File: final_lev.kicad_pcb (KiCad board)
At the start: 2 copper layers, 60 parts, among them Q1 IRF100B201, Q2 IRF100B201, Q3 IRF100B201, Q4 IRF100B201, U1 IR2184, U2 IR2184, U3 INA240A1D, U4 LM393, U5 74HC74

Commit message: clean rollback
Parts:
- added C101: 470uF, Capacitor_THT:CP_Radial_D18.0mm_P7.50mm, F.Cu at (30.1, 42.8)
- added C102: 470uF, Capacitor_THT:CP_Radial_D18.0mm_P7.50mm, F.Cu at (30.1, 62.3)
- added C103: 470uF, Capacitor_THT:CP_Radial_D18.0mm_P7.50mm, F.Cu at (30.1, 81.9)
- added C104: 470uF, Capacitor_THT:CP_Radial_D18.0mm_P7.50mm, F.Cu at (30.1, 101.4)
- added C105: 470uF, Capacitor_THT:CP_Radial_D18.0mm_P7.50mm, F.Cu at (30.1, 121.0)
- added C106: 470uF, Capacitor_THT:CP_Radial_D18.0mm_P7.50mm, F.Cu at (30.1, 140.5)
- added C201: 220uF, Capacitor_THT:CP_Radial_D8.0mm_P3.50mm, F.Cu at (120.4, 49.7)
- added C202: 220uF, Capacitor_THT:CP_Radial_D8.0mm_P3.50mm, F.Cu at (120.4, 59.3)
- added C203: 10uF, Capacitor_SMD:C_1206_3216Metric_Pad1.33x1.80mm_HandSolder, F.Cu at (120.2, 84.1)
- added C204: 100nF, Capacitor_SMD:C_0805_2012Metric_Pad1.18x1.45mm_HandSolder, F.Cu at (114.7, 46.5)
- added C205: 100nF, Capacitor_SMD:C_0805_2012Metric_Pad1.18x1.45mm_HandSolder, F.Cu at (114.7, 49.5)
- added C206: 100nF, Capacitor_SMD:C_0805_2012Metric_Pad1.18x1.45mm_HandSolder, F.Cu at (114.7, 52.5)
- added C207: 100nF, Capacitor_SMD:C_0805_2012Metric_Pad1.18x1.45mm_HandSolder, F.Cu at (114.7, 55.5)
- added C208: 100nF, Capacitor_SMD:C_0805_2012Metric_Pad1.18x1.45mm_HandSolder, F.Cu at (114.7, 58.5)
- added C209: 100nF, Capacitor_SMD:C_0805_2012Metric_Pad1.18x1.45mm_HandSolder, F.Cu at (114.7, 61.5)
- added C210: 100nF, Capacitor_SMD:C_0805_2012Metric_Pad1.18x1.45mm_HandSolder, F.Cu at (114.7, 64.5)
- added C211: 1nF, Capacitor_SMD:C_0805_2012Metric_Pad1.18x1.45mm_HandSolder, F.Cu at (105.0, 112.7)
- added C212: 1uF, Capacitor_SMD:C_1210_3225Metric_Pad1.33x2.70mm_HandSolder, F.Cu at (79.6, 92.6)
- added C213: 100nF, Capacitor_SMD:C_0805_2012Metric_Pad1.18x1.45mm_HandSolder, F.Cu at (105.0, 115.7)
- added C214: 1uF, Capacitor_SMD:C_1210_3225Metric_Pad1.33x2.70mm_HandSolder, F.Cu at (79.6, 96.9)
- added C215: 1uF, Capacitor_SMD:C_1210_3225Metric_Pad1.33x2.70mm_HandSolder, F.Cu at (79.6, 101.1)
- added C216: 1uF, Capacitor_SMD:C_1210_3225Metric_Pad1.33x2.70mm_HandSolder, F.Cu at (79.6, 105.4)
- added C217: 100nF, Capacitor_SMD:C_0805_2012Metric_Pad1.18x1.45mm_HandSolder, F.Cu at (105.0, 118.7)
- added C218: 100nF, Capacitor_SMD:C_0805_2012Metric_Pad1.18x1.45mm_HandSolder, F.Cu at (105.0, 121.7)
- added C219: 1uF, Capacitor_SMD:C_1210_3225Metric_Pad1.33x2.70mm_HandSolder, F.Cu at (79.6, 109.6)
- added C220: 1uF, Capacitor_SMD:C_1210_3225Metric_Pad1.33x2.70mm_HandSolder, F.Cu at (79.6, 113.9)
- added C221: 1uF, Capacitor_SMD:C_1210_3225Metric_Pad1.33x2.70mm_HandSolder, F.Cu at (79.6, 118.1)
- added C222: 1uF, Capacitor_SMD:C_1210_3225Metric_Pad1.33x2.70mm_HandSolder, F.Cu at (79.6, 122.4)
- added C223: 100nF, Capacitor_SMD:C_0805_2012Metric_Pad1.18x1.45mm_HandSolder, F.Cu at (105.0, 124.7)
- added C224: 100nF, Capacitor_SMD:C_0805_2012Metric_Pad1.18x1.45mm_HandSolder, F.Cu at (109.8, 112.7)
- added C225: 100nF, Capacitor_SMD:C_0805_2012Metric_Pad1.18x1.45mm_HandSolder, F.Cu at (109.8, 115.7)
- added C226: 1uF, Capacitor_SMD:C_0805_2012Metric_Pad1.18x1.45mm_HandSolder, F.Cu at (109.8, 118.7)
- added C227: 1uF, Capacitor_SMD:C_0805_2012Metric_Pad1.18x1.45mm_HandSolder, F.Cu at (109.8, 121.7)
- added C228: 100nF, Capacitor_SMD:C_0805_2012Metric_Pad1.18x1.45mm_HandSolder, F.Cu at (109.8, 124.7)
- added C229: 100nF, Capacitor_SMD:C_0805_2012Metric_Pad1.18x1.45mm_HandSolder, F.Cu at (114.6, 112.7)
- added C230: 1uF, Capacitor_SMD:C_0805_2012Metric_Pad1.18x1.45mm_HandSolder, F.Cu at (114.6, 115.7)
- added C231: 1uF, Capacitor_SMD:C_0805_2012Metric_Pad1.18x1.45mm_HandSolder, F.Cu at (114.6, 118.7)
- added D201: SS34, Diode_SMD:D_SMA_Handsoldering, F.Cu at (122.2, 66.3)
- added D202: SS34, Diode_SMD:D_SMA_Handsoldering, F.Cu at (122.2, 70.9)
- added D203: 1N4148W, Diode_SMD:D_SOD-123, F.Cu at (111.3, 92.2)
- added D204: 1N4148W, Diode_SMD:D_SOD-123, F.Cu at (111.3, 95.5)
- added D205: 5.0SMDJ70A, Diode_SMD:D_SMC_Handsoldering, F.Cu at (110.1, 130.1)
- added D206: 1N4148W, Diode_SMD:D_SOD-123, F.Cu at (111.3, 98.9)
- added D207: 1N4148W, Diode_SMD:D_SOD-123, F.Cu at (111.3, 102.2)
- added D208: ES1D, Diode_SMD:D_SMA_Handsoldering, F.Cu at (87.7, 116.6)
- added D209: ES1D, Diode_SMD:D_SMA_Handsoldering, F.Cu at (87.7, 121.1)
- added J101: +60V IN, lev_lib:389690002, F.Cu at (52.7, 40.6)
- added J201: RAILS IN, Connector_Molex:Molex_Micro-Fit_3.0_43650-0400_1x04_P3.00mm_Horizontal, F.Cu at (131.2, 54.9)
- added J202: CONTROL, Connector_Molex:Molex_Micro-Fit_3.0_43650-1200_1x12_P3.00mm_Horizontal, F.Cu at (111.9, 42.9)
- added J203: YOKE 1, lev_lib:389690002, F.Cu at (85.7, 40.6)
- added J204: YOKE 2, lev_lib:389690002, F.Cu at (85.7, 68.3)
- added Q201: IRF100B201, Package_TO_SOT_THT:TO-220-3_Vertical, F.Cu at (85.8, 94.4)
- added Q202: IRF100B201, Package_TO_SOT_THT:TO-220-3_Vertical, F.Cu at (85.8, 100.4)
- added Q203: IRF100B201, Package_TO_SOT_THT:TO-220-3_Vertical, F.Cu at (85.8, 106.3)
- added Q204: IRF100B201, Package_TO_SOT_THT:TO-220-3_Vertical, F.Cu at (85.8, 112.3)
- added R101: 22k, Resistor_SMD:R_1206_3216Metric_Pad1.30x1.75mm_HandSolder, F.Cu at (46.6, 62.4)
- added R201: 10k, Resistor_SMD:R_0805_2012Metric_Pad1.20x1.40mm_HandSolder, F.Cu at (110.0, 46.4)
- added R202: 10k, Resistor_SMD:R_0805_2012Metric_Pad1.20x1.40mm_HandSolder, F.Cu at (110.0, 49.4)
- added R203: 10k, Resistor_SMD:R_0805_2012Metric_Pad1.20x1.40mm_HandSolder, F.Cu at (110.0, 52.3)
- added R204: 10k, Resistor_SMD:R_0805_2012Metric_Pad1.20x1.40mm_HandSolder, F.Cu at (110.0, 55.3)
- added R205: 100R, Resistor_SMD:R_0805_2012Metric_Pad1.20x1.40mm_HandSolder, F.Cu at (110.0, 58.2)
- added R206: 100R, Resistor_SMD:R_0805_2012Metric_Pad1.20x1.40mm_HandSolder, F.Cu at (110.0, 61.2)
- added R207: 100R, Resistor_SMD:R_0805_2012Metric_Pad1.20x1.40mm_HandSolder, F.Cu at (110.0, 64.1)
- added R208: 100R, Resistor_SMD:R_0805_2012Metric_Pad1.20x1.40mm_HandSolder, F.Cu at (110.0, 67.1)
- added R209: 100R, Resistor_SMD:R_0805_2012Metric_Pad1.20x1.40mm_HandSolder, F.Cu at (110.0, 70.0)
- added R210: 10R, Resistor_SMD:R_0805_2012Metric_Pad1.20x1.40mm_HandSolder, F.Cu at (96.5, 92.0)
- added R211: 10R, Resistor_SMD:R_0805_2012Metric_Pad1.20x1.40mm_HandSolder, F.Cu at (96.5, 94.9)
- added R212: 4.7R, Resistor_SMD:R_0805_2012Metric_Pad1.20x1.40mm_HandSolder, F.Cu at (96.5, 97.9)
- added R213: 4.7R, Resistor_SMD:R_0805_2012Metric_Pad1.20x1.40mm_HandSolder, F.Cu at (96.5, 100.8)
- added R214: 10R, Resistor_SMD:R_1206_3216Metric_Pad1.30x1.75mm_HandSolder, F.Cu at (117.2, 92.2)
- added R215: 10R, Resistor_SMD:R_1206_3216Metric_Pad1.30x1.75mm_HandSolder, F.Cu at (117.2, 95.5)
- added R216: 10k, Resistor_SMD:R_0805_2012Metric_Pad1.20x1.40mm_HandSolder, F.Cu at (96.5, 103.8)
- added R217: 10k, Resistor_SMD:R_0805_2012Metric_Pad1.20x1.40mm_HandSolder, F.Cu at (96.5, 106.7)
- added R218: 10k, Resistor_SMD:R_0805_2012Metric_Pad1.20x1.40mm_HandSolder, F.Cu at (96.5, 109.7)
- added R219: 1m, Resistor_SMD:R_Shunt_Vishay_WSK2512_6332Metric_T2.66mm, F.Cu at (113.3, 106.3)
- added R220: 24k, Resistor_SMD:R_0805_2012Metric_Pad1.20x1.40mm_HandSolder, F.Cu at (101.3, 92.0)
- added R221: 10k, Resistor_SMD:R_0805_2012Metric_Pad1.20x1.40mm_HandSolder, F.Cu at (101.3, 94.9)
- added R222: 10k, Resistor_SMD:R_0805_2012Metric_Pad1.20x1.40mm_HandSolder, F.Cu at (101.3, 97.9)
- added R223: 10k, Resistor_SMD:R_0805_2012Metric_Pad1.20x1.40mm_HandSolder, F.Cu at (101.3, 100.8)
- added R224: 10k, Resistor_SMD:R_0805_2012Metric_Pad1.20x1.40mm_HandSolder, F.Cu at (101.3, 103.8)
- added R225: 10k, Resistor_SMD:R_0805_2012Metric_Pad1.20x1.40mm_HandSolder, F.Cu at (101.3, 106.7)
- added R226: 10R, Resistor_SMD:R_1206_3216Metric_Pad1.30x1.75mm_HandSolder, F.Cu at (117.2, 98.8)
- added R227: 10R, Resistor_SMD:R_1206_3216Metric_Pad1.30x1.75mm_HandSolder, F.Cu at (117.2, 102.1)
- added R228: 4.7R, Resistor_SMD:R_0805_2012Metric_Pad1.20x1.40mm_HandSolder, F.Cu at (101.3, 109.7)
- added R229: 4.7R, Resistor_SMD:R_0805_2012Metric_Pad1.20x1.40mm_HandSolder, F.Cu at (106.0, 92.0)
- added R230: 10k, Resistor_SMD:R_0805_2012Metric_Pad1.20x1.40mm_HandSolder, F.Cu at (106.0, 94.9)
- added R231: 1R, Resistor_SMD:R_0805_2012Metric_Pad1.20x1.40mm_HandSolder, F.Cu at (106.0, 97.9)
- added R232: 1R, Resistor_SMD:R_0805_2012Metric_Pad1.20x1.40mm_HandSolder, F.Cu at (106.0, 100.8)
- added U201: 74LVC2G17, Package_TO_SOT_SMD:SOT-23-6, F.Cu at (119.7, 75.6)
- added U202: 74LVC2G17, Package_TO_SOT_SMD:SOT-23-6, F.Cu at (119.7, 80.2)
- added U203: INA240A1D, Package_SO:SOIC-8_3.9x4.9mm_P1.27mm, F.Cu at (98.4, 114.5)
- added U204: LM393, Package_SO:SOIC-8_3.9x4.9mm_P1.27mm, F.Cu at (98.4, 121.1)
- added U205: 74HC74, Package_SO:SOIC-14_3.9x8.7mm_P1.27mm, F.Cu at (86.8, 128.7)
- added U206: IR2184, Package_SO:SOIC-8_3.9x4.9mm_P1.27mm, F.Cu at (98.4, 127.7)
- added U207: IR2184, Package_SO:SOIC-8_3.9x4.9mm_P1.27mm, F.Cu at (98.4, 134.3)
- moved C16 89.6 mm to (155.4, 112.7)
- moved C17 89.6 mm to (155.4, 115.7)
- moved C18 89.6 mm to (155.4, 118.7)
- moved C19 89.6 mm to (155.4, 121.7)
- moved C20 89.6 mm to (155.4, 124.7)
- moved C21 89.6 mm to (160.2, 112.7)
- moved C22 89.6 mm to (160.2, 115.7)
- moved C23 89.6 mm to (160.2, 118.7)
- moved D5 89.6 mm to (156.9, 95.5)
- moved R9 89.6 mm to (162.7, 98.8)
- moved U1 89.6 mm to (143.9, 114.5)
- moved U2 89.6 mm to (143.9, 121.1)
- moved U3 89.6 mm to (143.9, 127.7)
- moved U4 89.6 mm to (143.9, 134.3)
- moved C1 89.6 mm to (150.6, 112.7)
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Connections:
- net /power_channel/FAULT_N renamed /CH1/FAULT_N
- net /power_channel/G_Q1 renamed /CH1/G_Q1
- net /power_channel/G_Q2 renamed /CH1/G_Q2
- net /power_channel/G_Q3 renamed /CH1/G_Q3
- net /power_channel/G_Q4 renamed /CH1/G_Q4
- net /power_channel/HO_A renamed /CH1/HO_A
- net /power_channel/HO_B renamed /CH1/HO_B
- net /power_channel/ISNS renamed /ISNS1
- net /power_channel/LO_A renamed /CH1/LO_A
- net /power_channel/LO_B renamed /CH1/LO_B
- net /power_channel/RESET renamed /RESET
- net /power_channel/SD renamed /CH1/SD
- net /power_channel/SNS_N renamed /CH1/SNS_N
- net /power_channel/SNS_N_F renamed /CH1/SNS_N_F
- net /power_channel/SNS_P renamed /CH1/SNS_P
- net /power_channel/SNS_P_F renamed /CH1/SNS_P_F
- net /power_channel/SW_A renamed /CH1/SW_A
- net /power_channel/SW_B renamed /COIL_B1
- net /power_channel/VB_A renamed /CH1/VB_A
- net /power_channel/VB_B renamed /CH1/VB_B
- net /power_channel/VTH_HI renamed /CH1/VTH_HI
- net /power_channel/VTH_LO renamed /CH1/VTH_LO
- R11 pad 4: /power_channel/COIL_A -> /COIL_A1
- U1 pad 1: /power_channel/PWM_A -> /PWM_A1
- U2 pad 1: /power_channel/PWM_B -> /PWM_B1
- U5 pad 5: /power_channel/FAULT -> /FAULT1

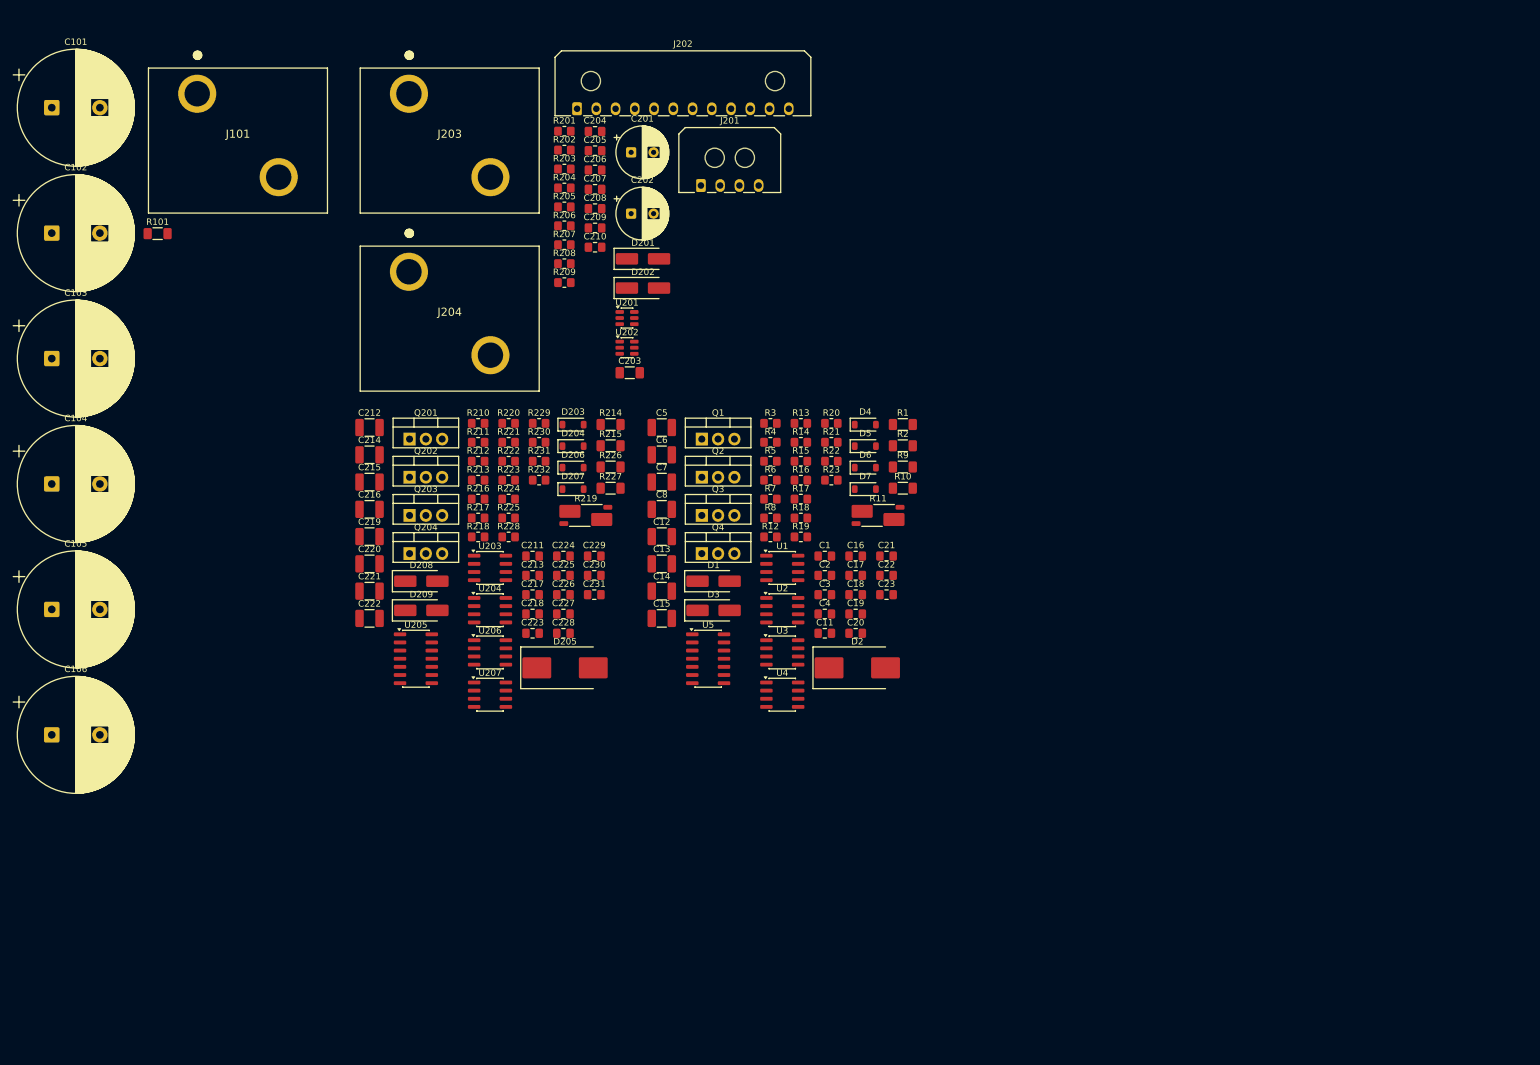
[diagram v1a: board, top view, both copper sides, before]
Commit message: Adversarial review fixes: set-dominant latch, MCU enable, 3V3 hold-up, sense chain, 16-way connector
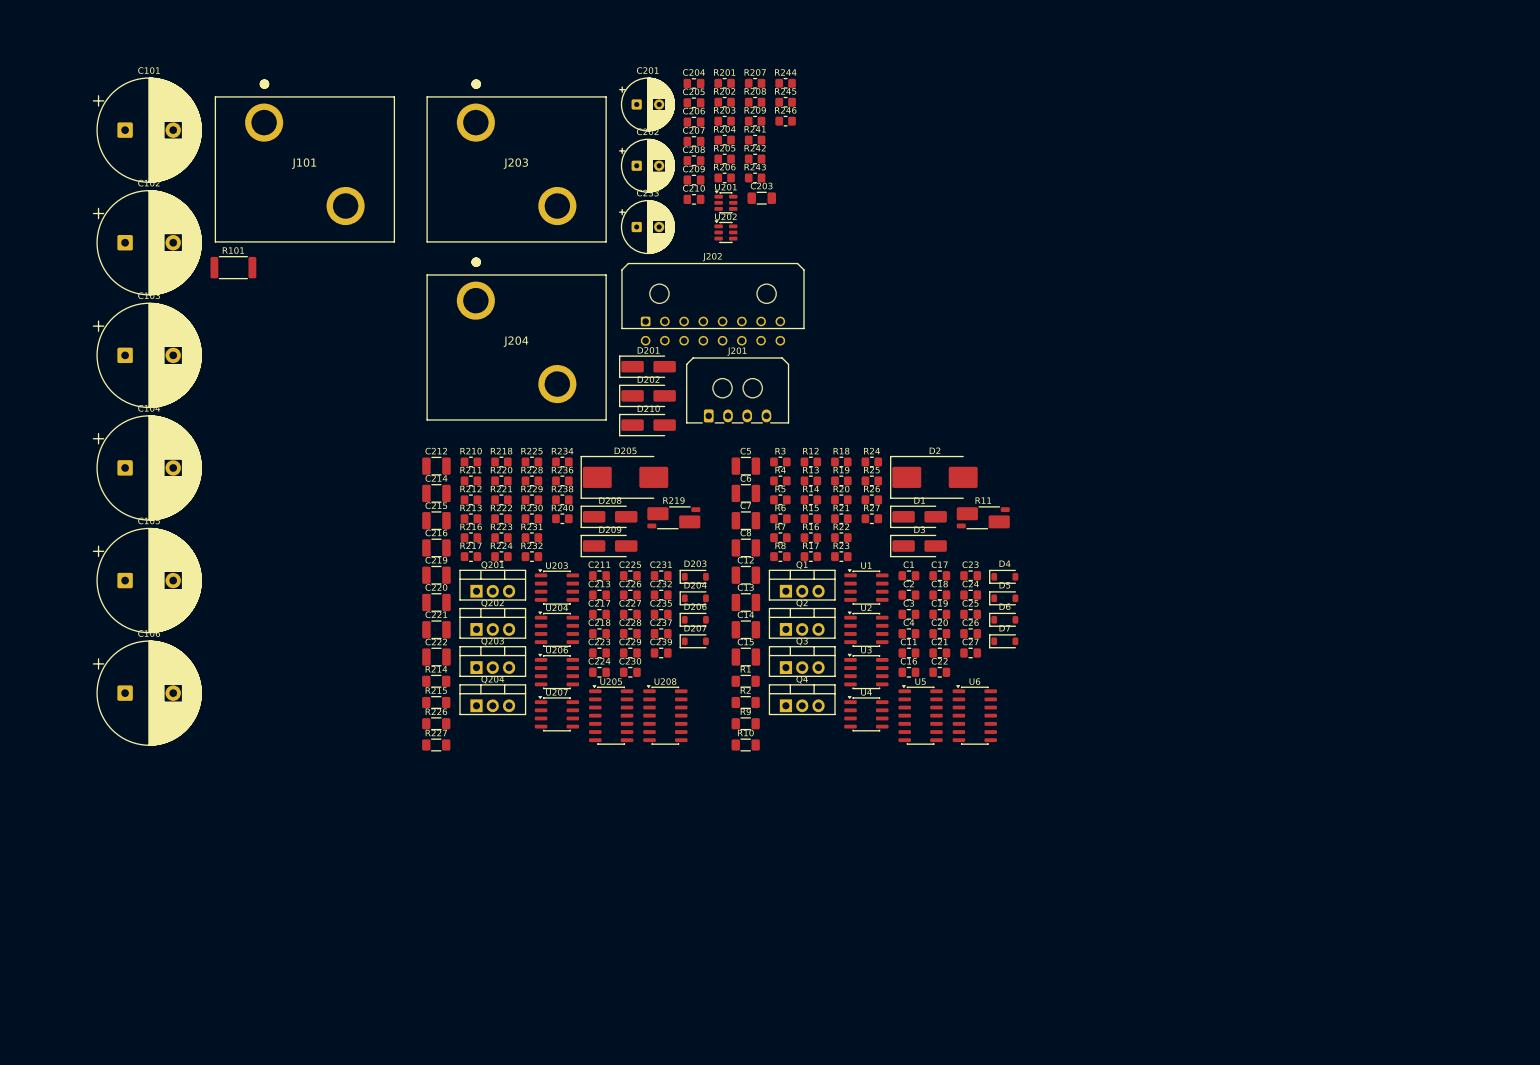
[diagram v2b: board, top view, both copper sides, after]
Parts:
- added C232: 100nF, Capacitor_SMD:C_0805_2012Metric_Pad1.18x1.45mm_HandSolder, F.Cu at (125.1, 118.7)
- added C233: 220uF, Capacitor_THT:CP_Radial_D8.0mm_P3.50mm, F.Cu at (121.2, 61.4)
- added C235: 100nF, Capacitor_SMD:C_0805_2012Metric_Pad1.18x1.45mm_HandSolder, F.Cu at (125.1, 121.7)
- added C237: 100nF, Capacitor_SMD:C_0805_2012Metric_Pad1.18x1.45mm_HandSolder, F.Cu at (125.1, 124.8)
- added C239: 4.7nF, Capacitor_SMD:C_0805_2012Metric_Pad1.18x1.45mm_HandSolder, F.Cu at (125.1, 127.8)
- added C24: 100nF, Capacitor_SMD:C_0805_2012Metric_Pad1.18x1.45mm_HandSolder, F.Cu at (173.3, 118.7)
- added C25: 100nF, Capacitor_SMD:C_0805_2012Metric_Pad1.18x1.45mm_HandSolder, F.Cu at (173.3, 121.7)
- added C26: 100nF, Capacitor_SMD:C_0805_2012Metric_Pad1.18x1.45mm_HandSolder, F.Cu at (173.3, 124.8)
- added C27: 4.7nF, Capacitor_SMD:C_0805_2012Metric_Pad1.18x1.45mm_HandSolder, F.Cu at (173.3, 127.8)
- added D210: SS34, Diode_SMD:D_SMA_Handsoldering, F.Cu at (123.1, 92.2)
- added R234: 3.3k, Resistor_SMD:R_0805_2012Metric_Pad1.20x1.40mm_HandSolder, F.Cu at (109.7, 98.0)
- added R236: 10k, Resistor_SMD:R_0805_2012Metric_Pad1.20x1.40mm_HandSolder, F.Cu at (109.7, 100.9)
- added R238: 10k, Resistor_SMD:R_0805_2012Metric_Pad1.20x1.40mm_HandSolder, F.Cu at (109.7, 103.9)
- added R24: 10k, Resistor_SMD:R_0805_2012Metric_Pad1.20x1.40mm_HandSolder, F.Cu at (157.9, 98.0)
- added R240: 1k, Resistor_SMD:R_0805_2012Metric_Pad1.20x1.40mm_HandSolder, F.Cu at (109.7, 106.8)
- added R241: 15k, Resistor_SMD:R_0805_2012Metric_Pad1.20x1.40mm_HandSolder, F.Cu at (139.7, 47.8)
- added R242: 15k, Resistor_SMD:R_0805_2012Metric_Pad1.20x1.40mm_HandSolder, F.Cu at (139.7, 50.8)
- added R243: 100R, Resistor_SMD:R_0805_2012Metric_Pad1.20x1.40mm_HandSolder, F.Cu at (139.7, 53.7)
- added R244: 10k, Resistor_SMD:R_0805_2012Metric_Pad1.20x1.40mm_HandSolder, F.Cu at (144.4, 39.0)
- added R245: 100R, Resistor_SMD:R_0805_2012Metric_Pad1.20x1.40mm_HandSolder, F.Cu at (144.4, 41.9)
- added R246: 10k, Resistor_SMD:R_0805_2012Metric_Pad1.20x1.40mm_HandSolder, F.Cu at (144.4, 44.9)
- added R25: 10k, Resistor_SMD:R_0805_2012Metric_Pad1.20x1.40mm_HandSolder, F.Cu at (157.9, 100.9)
- added R26: 3.3k, Resistor_SMD:R_0805_2012Metric_Pad1.20x1.40mm_HandSolder, F.Cu at (157.9, 103.9)
- added R27: 1k, Resistor_SMD:R_0805_2012Metric_Pad1.20x1.40mm_HandSolder, F.Cu at (157.9, 106.8)
- added U208: 74HCT00, Package_SO:SOIC-14_3.9x8.7mm_P1.27mm, F.Cu at (125.7, 137.5)
- added U6: 74HCT00, Package_SO:SOIC-14_3.9x8.7mm_P1.27mm, F.Cu at (173.9, 137.5)
- C101, C102, C103, C104, C105, C106: footprint Capacitor_THT:CP_Radial_D18.0mm_P7.50mm -> Capacitor_THT:CP_Radial_D16.0mm_P7.50mm
- J202: value CONTROL -> Conn_02x08_Odd_Even; footprint Connector_Molex:Molex_Micro-Fit_3.0_43650-1200_1x12_P3.00mm_Horizontal -> Connector_Molex:Molex_Micro-Fit_3.0_43045-1600_2x08_P3.00mm_Horizontal
- R101: footprint Resistor_SMD:R_1206_3216Metric_Pad1.30x1.75mm_HandSolder -> Resistor_SMD:R_2512_6332Metric
- R11, R219: value 1m -> 0.5m
- R15, R220: value 24k -> 43k
- R206, R207: value 100R -> 10k
- U203, U3: value INA240A1D -> INA240A2D
- U204, U4: value LM393 -> LM2903B
- U205, U5: value 74HC74 -> 74HCT74
- moved R214 48.4 mm to (90.0, 132.2)
- moved R215 48.4 mm to (90.0, 135.5)
- moved R227 48.4 mm to (90.0, 142.1)
- moved R226 48.4 mm to (90.0, 138.8)
- moved R1 46.9 mm to (138.2, 132.2)
- moved R2 46.9 mm to (138.2, 135.5)
- moved R10 46.9 mm to (138.2, 142.1)
- moved R9 46.9 mm to (138.2, 138.8)
- moved R207 38.9 mm to (139.7, 39.0)
- moved R208 38.9 mm to (139.7, 41.9)
- moved R209 38.9 mm to (139.7, 44.9)
- moved J201 35.9 mm to (132.5, 90.8)
- moved J202 34.8 mm to (122.6, 76.1)
- moved U5 34.3 mm to (165.5, 137.5)
- moved C203 34.1 mm to (140.7, 56.9)
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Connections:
- J201 pad 3: +3.3V -> /IO_PROTECT/+3V3_IN
- J202 pad 10: /IO_PROTECT/ISNS1_OUT -> /IO_PROTECT/EN2_IN
- J202 pad 11: /IO_PROTECT/ISNS2_OUT -> /IO_PROTECT/RESET_IN
- J202 pad 12: GND -> /IO_PROTECT/OK1_OUT
- J202 pad 2: /IO_PROTECT/PWM_A1_IN -> GND
- J202 pad 3: /IO_PROTECT/PWM_B1_IN -> /IO_PROTECT/PWM_A1_IN
- J202 pad 5: /IO_PROTECT/PWM_B2_IN -> /IO_PROTECT/PWM_B1_IN
- J202 pad 6: GND -> /IO_PROTECT/PWM_B2_IN
- J202 pad 7: /IO_PROTECT/RESET_IN -> GND
- J202 pad 8: /IO_PROTECT/FAULT1_OUT -> GND
- J202 pad 9: /IO_PROTECT/FAULT2_OUT -> /IO_PROTECT/EN1_IN
- R206 pad 1: /IO_PROTECT/FAULT1_OUT -> /IO_PROTECT/OK1_OUT
- R206 pad 2: /FAULT1 -> /OK1
- R207 pad 1: /IO_PROTECT/FAULT2_OUT -> /IO_PROTECT/OK2_OUT
- R207 pad 2: /FAULT2 -> /OK2
- U204 pad 2: /ISNS2 -> /CH2/ISNS_F
- U204 pad 5: /ISNS2 -> /CH2/ISNS_F
- U205 pad 1: /RESET -> /CH2/RESET_EFF
- U205 pad 5: /FAULT2 -> unconnected-(U205A-Q-Pad5)
- U205 pad 6: /CH2/SD -> /CH2/SD_Q
- U4 pad 2: /ISNS1 -> /CH1/ISNS_F
- U4 pad 5: /ISNS1 -> /CH1/ISNS_F
- U5 pad 1: /RESET -> /CH1/RESET_EFF
- U5 pad 5: /FAULT1 -> unconnected-(U5A-Q-Pad5)
- U5 pad 6: /CH1/SD -> /CH1/SD_Q

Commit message: A14 modulation commitment (unipolar 3-level, 180 deg interleave); title blocks refreshed
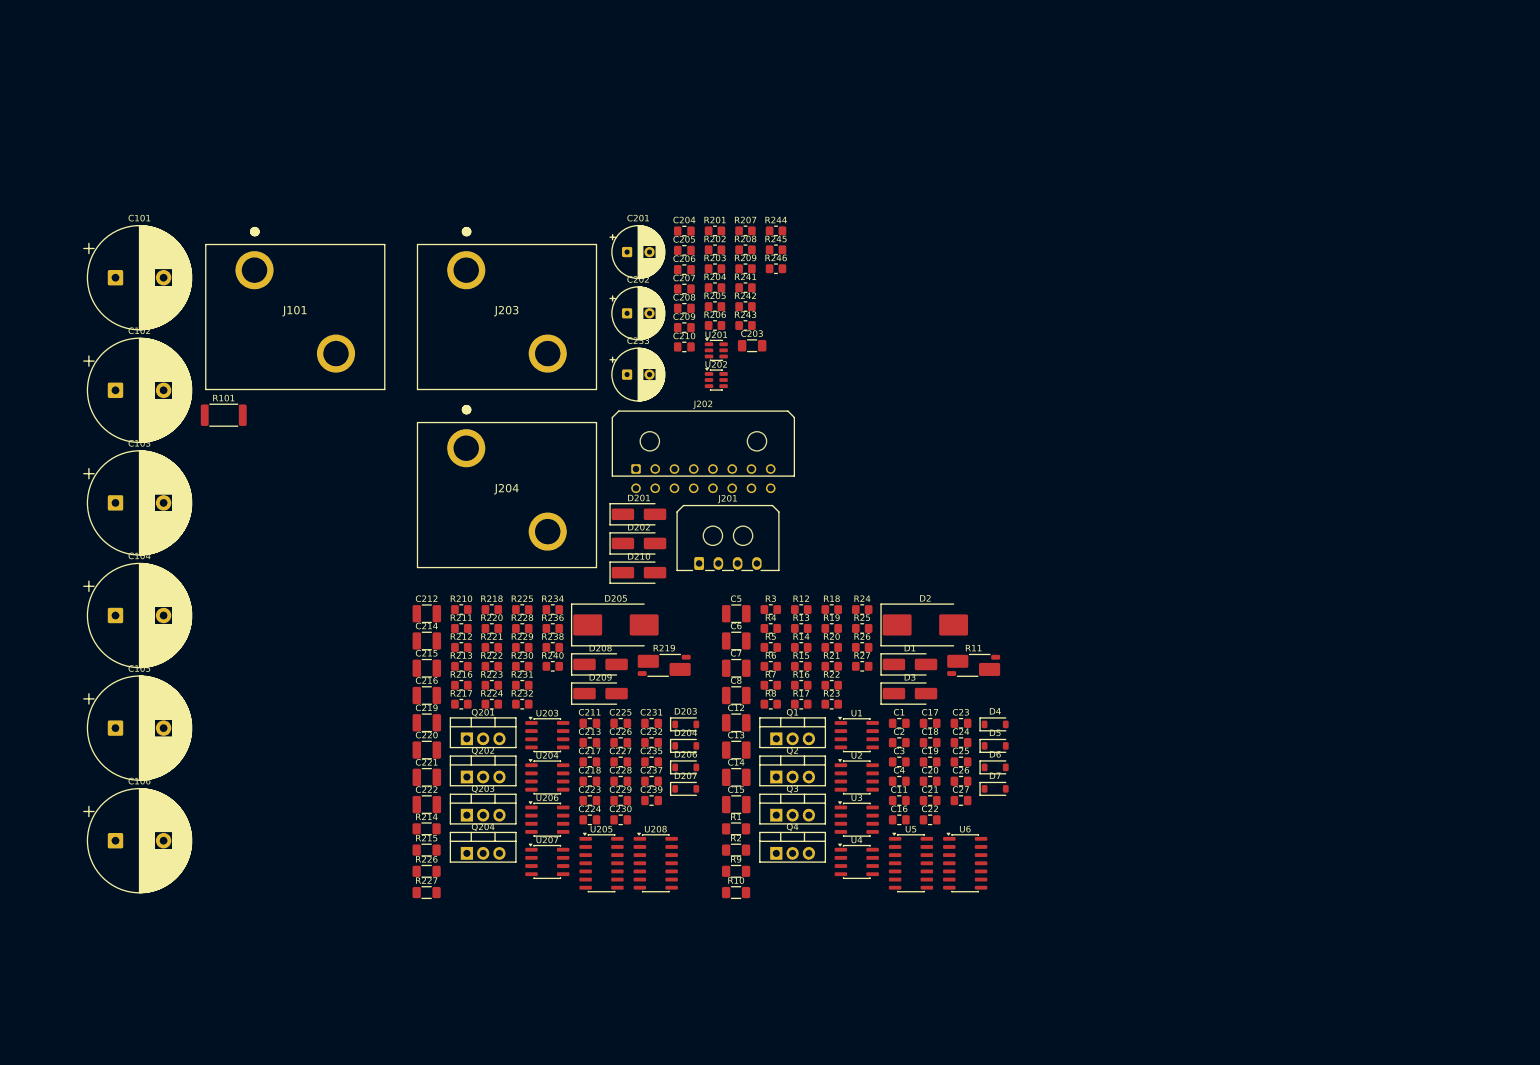
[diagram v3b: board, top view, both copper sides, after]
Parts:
- moved C12 23.0 mm to (136.8, 138.6)
- moved C13 23.0 mm to (136.8, 142.9)
- moved C14 23.0 mm to (136.8, 147.1)
- moved C18 23.0 mm to (167.0, 141.7)
- moved C2 23.0 mm to (162.2, 141.7)
- moved C213 23.0 mm to (113.9, 141.7)
- moved C215 23.0 mm to (88.5, 130.1)
- moved C216 23.0 mm to (88.5, 134.4)
- moved C219 23.0 mm to (88.5, 138.6)
- moved C220 23.0 mm to (88.5, 142.9)
- moved C221 23.0 mm to (88.5, 147.1)
- moved C226 23.0 mm to (118.7, 141.7)
- moved C232 23.0 mm to (123.6, 141.7)
- moved C24 23.0 mm to (171.8, 141.7)
- moved C7 23.0 mm to (136.8, 130.1)
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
